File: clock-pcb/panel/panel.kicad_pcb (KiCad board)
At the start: 2 copper layers, 69.4 x 89.9 mm, 94 parts, among them J1 Conn_01x03_Pin, J1 Conn_01x07_Socket, J1 USB4140-GF-0070-C, J10 Conn_01x01_Socket, J11 Conn_01x01_Socket, J12 Conn_01x01_Socket, J13 Conn_01x01_Socket, J14 Conn_01x01_Socket, J15 Conn_01x02_Socket, J2 Conn_01x01_Pin, J2 oled, J3 Led display, J4 Led display 2, J5 Conn_01x07_Socket, J6 Conn_01x07_Socket, J7 Conn_01x01_Socket, J8 Conn_01x02_Socket, J9 Conn_01x01_Socket, Q1 FS8205A, Q2 FDN304PZ, U1 BH1750FVI-TR, U1 ESP32-WROOM-E, U1 TMAG5231C1GQDBZR, U3 OPT3004DTSR, U4 SHT4x, U4 TPS2116DRL, U5 MCP73811T-420I-OT, U7 TLV75533PDBV

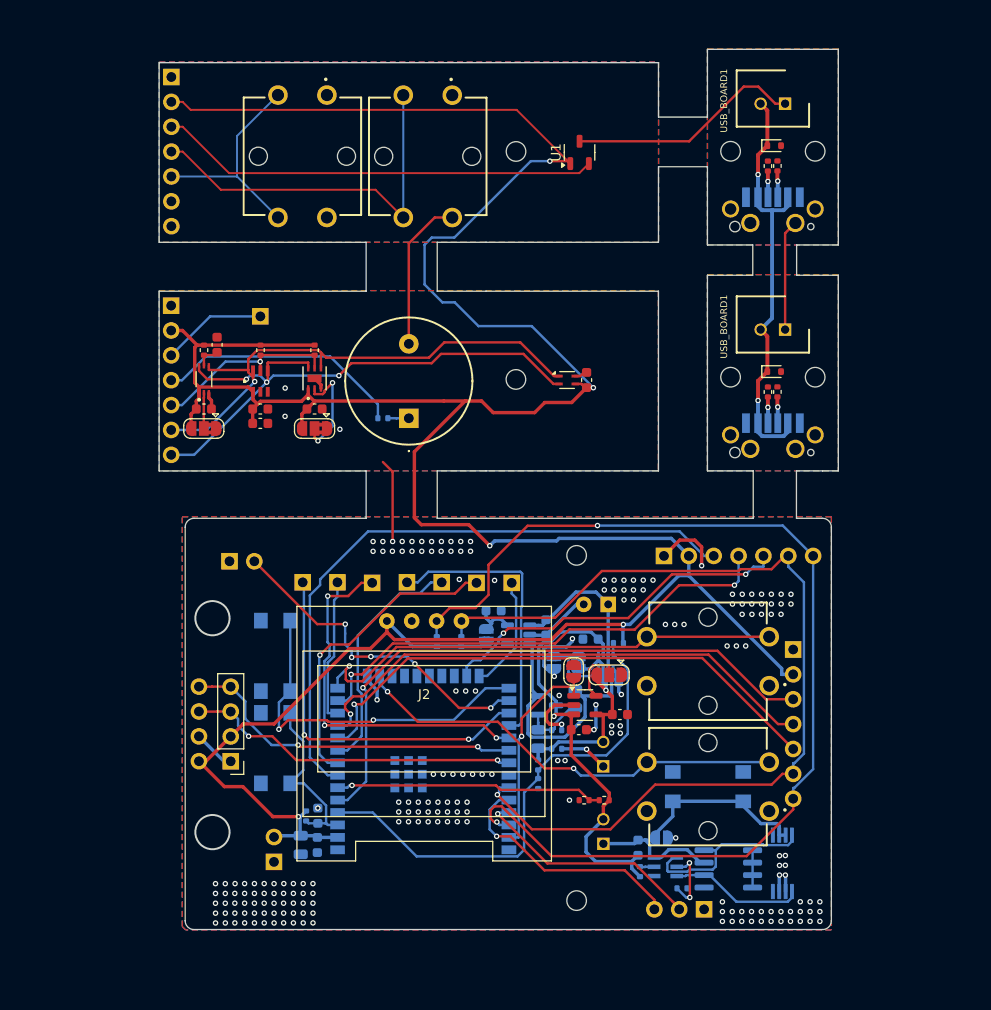
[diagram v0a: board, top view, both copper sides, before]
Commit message: voltage regulator
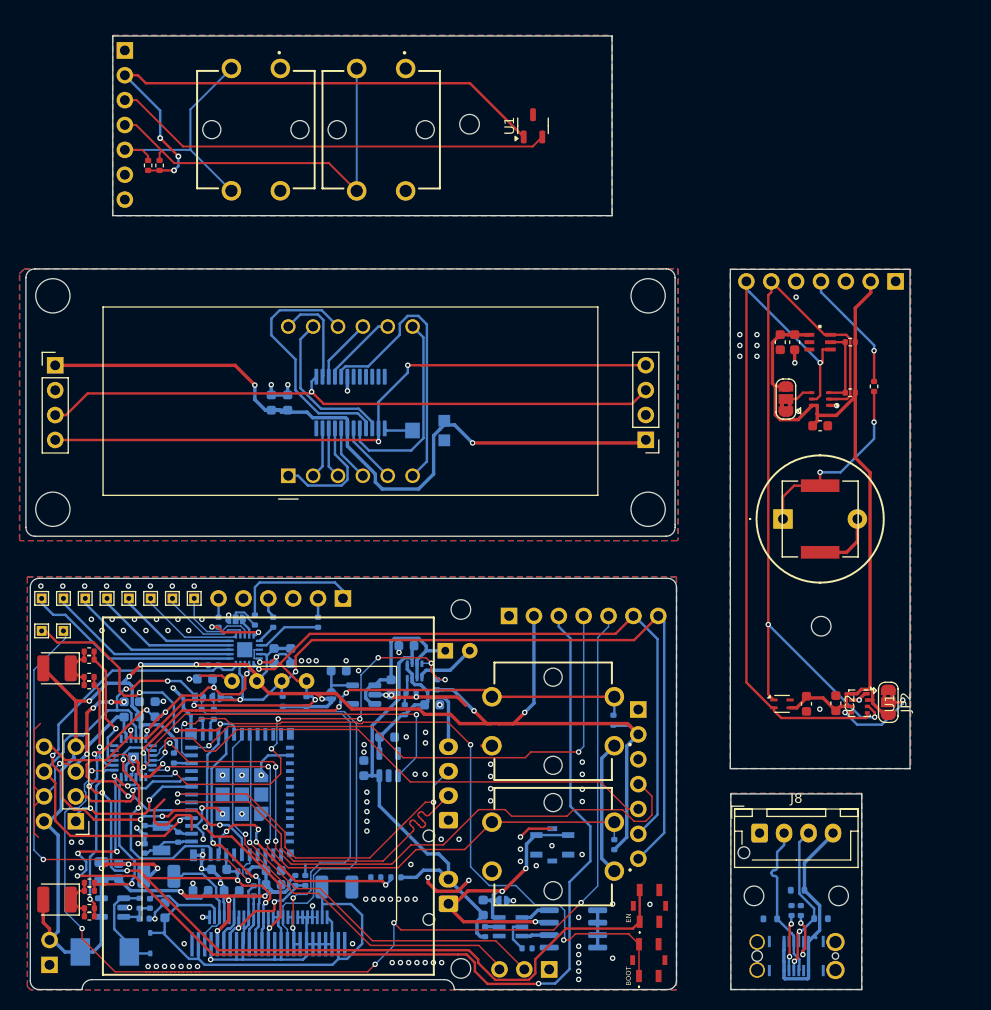
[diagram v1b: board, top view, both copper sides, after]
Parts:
- removed BATT_P1, BOOT1, EN1: TL3305AF160QG, clock:TL3305AF160QG
- removed the C1 at (110.3, 82.2)
- removed the C1 at (118.9, 133.3)
- removed the C2 at (109.0, 88.8)
- removed the C2 at (120.6, 133.3)
- removed the C3 at (114.8, 88.8)
- removed the C3 at (120.6, 130.3)
- removed the C4 at (114.8, 90.3)
- removed the C4 at (153.3, 133.6)
- removed the C5 at (120.3, 88.8)
- removed the C5 at (150.3, 108.8)
- removed the C6 at (148.1, 85.8)
- removed the C6 at (150.6, 116.7)
- removed the D1 at (167.2, 85.0)
- removed the D1 at (167.2, 61.9)
- removed the D3 at (143.1, 122.5)
- removed D4: SD0805S040S0R5, Diode_SMD:D_0805_2012Metric
- removed the J1 at (167.1, 68.6)
- removed the J1 at (167.1, 91.7)
- removed the J1 at (105.7, 78.2)
- removed the J1 at (105.7, 54.9)
- removed the J1 at (160.1, 139.9)
- removed J10, J12, J13, J14: Conn_01x01_Socket, Connector_PinSocket_2.54mm:PinSocket_1x01_P2.54mm_Vertical
- removed the J2 at (118.5, 134.9)
- removed the J2 at (114.8, 79.3)
- removed the J8 at (111.6, 104.3)
- removed the JP1 at (109.0, 90.8)
- removed the JP1 at (155.7, 132.6)
- removed the JP2 at (120.3, 90.8)
- removed the JP2 at (144.7, 114.7)
- removed JP3: Jumper_bridged, Jumper:SolderJumper-2_P1.3mm_Bridged2Bar_RoundedPad1.0x1.5mm
- removed JP4: SolderJumper_3_Open, Jumper:SolderJumper-3_P1.3mm_Open_RoundedPad1.0x1.5mm
- removed the L1 at (129.9, 89.7)
- removed Q1: FS8205A, clock:SOP65P640X120-8N
- removed Q2: FDN304PZ, Package_TO_SOT_SMD:SOT-23
- removed the R1 at (167.6, 64.0)
- removed the R1 at (109.0, 82.8)
- removed the R1 at (167.6, 87.0)
- removed the R1 at (119.4, 130.4)
- removed the R11 at (132.8, 112.5)
- removed the R2 at (166.6, 64.0)
- removed the R2 at (149.9, 128.8)
- removed the R2 at (166.6, 87.1)
- removed the R2 at (114.8, 82.8)
- removed the R3 at (120.3, 82.8)
- removed the R3 at (147.8, 128.8)
- removed the R4 at (127.3, 89.7)
- removed the R4 at (153.5, 136.1)
- removed the S1 at (119.1, 63.0)
- removed the S2 at (131.9, 63.0)
- removed the U1 at (109.0, 85.8)
- removed the U1 at (147.4, 62.6)
- removed the U1 at (131.4, 126.8)
- removed the U2 at (114.8, 85.9)
- removed the U2 at (156.1, 135.6)
- removed the U3 at (120.3, 85.7)
- removed the U3 at (149.8, 133.2)
- removed the U4 at (146.1, 85.8)
- removed the U4 at (150.0, 114.6)
- removed USB_BOARD1 (x3): Conn_01x02_Socket, clock:SHDR2W64P0X250_1X2_740X575X700P
- added C1: 0.1uF, Capacitor_SMD:C_0603_1608Metric, F.Cu at (171.9, 90.5)
- added C1: 0.1uF, Capacitor_SMD:C_0603_1608Metric, B.Cu at (116.2, 114.0)
- added C12: 1uF, Capacitor_SMD:C_0603_1608Metric, B.Cu at (104.0, 119.5)
- added C13: 1uF, Capacitor_SMD:C_0603_1608Metric, B.Cu at (110.5, 135.8)
- added C14: 1uF, Capacitor_SMD:C_0603_1608Metric, B.Cu at (109.1, 116.4)
- added C15: 1uF, Capacitor_SMD:C_0603_1608Metric, B.Cu at (117.9, 114.0)
- added C16: 4.7uF, Capacitor_SMD:C_0805_2012Metric, B.Cu at (98.5, 136.0)
- added C17: 10uF, Capacitor_SMD:C_0603_1608Metric, B.Cu at (105.0, 140.0)
- added C18: 6.4pF, Capacitor_SMD:C_0402_1005Metric, B.Cu at (103.5, 139.3)
- added C19: 19pF, Capacitor_SMD:C_0402_1005Metric, B.Cu at (103.0, 131.8)
- added C2: 0.1uF, Capacitor_SMD:C_0603_1608Metric, F.Cu at (173.5, 118.8)
- added C2: 0.1uF, Capacitor_SMD:C_0603_1608Metric, B.Cu at (100.8, 119.5)
- added C20: 19pF, Capacitor_SMD:C_0402_1005Metric, B.Cu at (103.0, 133.7)
- added C21: 1uF, Capacitor_SMD:C_0603_1608Metric, B.Cu at (100.3, 136.0)
- added C23: 0.1uF, Capacitor_SMD:C_0603_1608Metric, B.Cu at (117.5, 88.1)
- added C23: 0.1uF, Capacitor_SMD:C_0603_1608Metric, B.Cu at (116.1, 135.9)
- added C24: 10uF, Capacitor_SMD:C_0603_1608Metric, B.Cu at (115.9, 88.1)
- added C24: 10uF, Capacitor_SMD:C_0603_1608Metric, B.Cu at (116.1, 137.4)
- added C25: 1uF, Capacitor_SMD:C_0603_1608Metric, B.Cu at (111.8, 138.0)
- added C26: 4.7uF, Capacitor_Tantalum_SMD:CP_EIA-3528-12_Kemet-T, B.Cu at (104.4, 136.5)
- added C27: 4.7uF, Capacitor_Tantalum_SMD:CP_EIA-3528-12_Kemet-T, B.Cu at (122.6, 137.6)
- added C28: 1uF, Capacitor_SMD:C_0603_1608Metric, B.Cu at (108.7, 138.0)
- added C3: 0.1uF, Capacitor_SMD:C_0603_1608Metric, F.Cu at (169.3, 82.0)
- added C3: 10uF, Capacitor_SMD:C_0603_1608Metric, B.Cu at (102.4, 119.5)
- added C4: 4.7uF, Capacitor_SMD:C_0603_1608Metric, F.Cu at (167.9, 82.0)
- added C4: 0.1uF, Capacitor_SMD:C_0603_1608Metric, B.Cu at (137.5, 139.7)
- added C5: 100uF, Capacitor_THT:CP_Radial_D5.0mm_P2.50mm, B.Cu at (133.6, 113.5)
- added C6: 0.1uF, Capacitor_SMD:C_0603_1608Metric, F.Cu at (170.5, 118.9)
- added C6: 1uF, Capacitor_SMD:C_0603_1608Metric, B.Cu at (132.3, 119.0)
- added D1: LED, LED_SMD:LED_1210_3225Metric, F.Cu at (94.0, 138.9)
- added D1: ESD5Zxx, Diode_SMD:D_SOD-523, B.Cu at (169.6, 138.0)
- added D2: LED, LED_SMD:LED_1210_3225Metric, F.Cu at (94.0, 115.3)
- added D2: ESD5Zxx, Diode_SMD:D_SOD-523, B.Cu at (166.8, 140.9)
- added D3: ESD5Zxx, Diode_SMD:D_SOD-523, B.Cu at (172.0, 140.9)
- added D3: NSVR0340HT1G, Diode_SMD:D_SOD-323, B.Cu at (103.5, 143.4)
- added IC1: VEML6030-GS15, clock:VEML6030GS15, F.Cu at (171.9, 87.8)
- added IC2: MCP23018-E_MJ, clock:QFN50P400X400X90-25N-D, B.Cu at (101.8, 124.4)
- added J1: Conn_01x04_Socket, Connector_PinHeader_2.54mm:PinHeader_1x04_P2.54mm_Vertical, F.Cu at (93.8, 84.3)
- added J1: Conn_01x03_Pin, Connector_PinHeader_2.54mm:PinHeader_1x03_P2.54mm_Vertical, B.Cu at (144.3, 146.0)
- added J1: Conn_01x07_Socket, Connector_PinHeader_2.54mm:PinHeader_1x07_P2.54mm_Horizontal, B.Cu at (179.6, 75.8)
- added J1: Conn_01x07_Socket, Connector_PinHeader_2.54mm:PinHeader_1x07_P2.54mm_Horizontal, B.Cu at (100.9, 52.2)
- added J1: USB4145-03-0070-C, clock:USB4145030070C, B.Cu at (169.5, 144.7)
- added J2: oled 2, clock:SSD1306_0.96_Oled, F.Cu at (102.7, 141.1)
- added J2: Conn_01x04_Socket, Connector_PinHeader_2.54mm:PinHeader_1x04_P2.54mm_Vertical, F.Cu at (154.1, 91.9)
- added J8: Conn_01x04_Socket, Connector_JST:JST_XH_B4B-XH-AM_1x04_P2.50mm_Vertical, F.Cu at (165.8, 132.1)
- added J8: SFV25R-2STE1HLF, clock:AMPHENOL_SFV25R-2STE1HLF, B.Cu at (115.6, 143.1)
- added JP1: SolderJumper_3_Bridged12, Jumper:SolderJumper-3_P1.3mm_Bridged2Bar12_RoundedPad1.0x1.5mm, F.Cu at (168.4, 87.8)
- added JP1: Jumper, clock:jumper_solder_small, B.Cu at (139.5, 139.0)
- added JP2: SolderJumper_3_Bridged12, Jumper:SolderJumper-3_P1.3mm_Bridged2Bar12_RoundedPad1.0x1.5mm, F.Cu at (178.9, 118.8)
- added JP2: SolderJumper_3_Bridged12, clock:jumper_solder_small_3_bridged, B.Cu at (112.2, 110.3)
- added JP6: Jumper, clock:jumper_solder_small, B.Cu at (110.3, 118.2)
- added L1: CPT-14146-80T, clock:CPT1414680T, F.Cu at (168.1, 100.0)
- added L1: 10uH 1A, clock:HPI0530-100, B.Cu at (98.9, 144.0)
- added LS1: Speaker_Crystal, clock:AST0760_MAL, F.Cu at (171.9, 100.0)
- added R0: 5.1k, Resistor_SMD:R_0402_1005Metric, B.Cu at (105.9, 124.5)
- added R1: 10K, Resistor_SMD:R_0402_1005Metric, F.Cu at (104.5, 63.9)
- added R1: 10K, Resistor_SMD:R_0402_1005Metric, F.Cu at (175.0, 87.1)
- added R1: 100k, Resistor_SMD:R_0402_1005Metric, B.Cu at (117.0, 118.7)
- added R1: 5.1k, Resistor_SMD:R_0402_1005Metric, B.Cu at (170.0, 140.0)
- added R11: 10K, Resistor_SMD:R_0402_1005Metric, F.Cu at (103.3, 63.9)
- added R11: 10K, Resistor_SMD:R_0402_1005Metric, B.Cu at (113.0, 136.0)
- added R13: 250k, Resistor_SMD:R_0402_1005Metric, B.Cu at (129.5, 119.5)
- added R14: 100k, Resistor_SMD:R_0402_1005Metric, B.Cu at (130.2, 117.8)
- added R15: 10K, Resistor_SMD:R_0402_1005Metric, B.Cu at (150.8, 120.6)
- added R16: 10K, Resistor_SMD:R_0402_1005Metric, B.Cu at (120.7, 110.6)
- added R17: 330, Resistor_SMD:R_0402_1005Metric, F.Cu at (97.3, 137.2)
- added R18: 330, Resistor_SMD:R_0402_1005Metric, F.Cu at (97.3, 140.6)
- added R19: 330, Resistor_SMD:R_0402_1005Metric, F.Cu at (97.3, 138.0)
- added R2: 10K, Resistor_SMD:R_0402_1005Metric, F.Cu at (175.0, 82.0)
- added R2: 300k, Resistor_SMD:R_0402_1005Metric, B.Cu at (128.6, 136.6)
- added R20: 330, Resistor_SMD:R_0402_1005Metric, F.Cu at (97.3, 139.8)
- added R21: 10M, Resistor_SMD:R_0402_1005Metric, B.Cu at (106.4, 132.5)
- added R22: 330, Resistor_SMD:R_0402_1005Metric, F.Cu at (97.3, 116.2)
- added R23: 330, Resistor_SMD:R_0402_1005Metric, F.Cu at (97.3, 117.0)
- added R24: 330, Resistor_SMD:R_0402_1005Metric, F.Cu at (97.3, 114.4)
- added R25: 330, Resistor_SMD:R_0402_1005Metric, F.Cu at (97.3, 113.6)
- added R26: 300k, Resistor_SMD:R_0402_1005Metric, B.Cu at (102.9, 140.8)
- added R27: 3.16M, Resistor_SMD:R_0402_1005Metric, B.Cu at (102.4, 139.3)
- added R28: 10K, Resistor_SMD:R_0402_1005Metric, B.Cu at (150.9, 133.3)
- added R29: 1.2M, Resistor_SMD:R_0402_1005Metric, B.Cu at (114.1, 138.0)
- added R3: 800k, Resistor_SMD:R_0402_1005Metric, B.Cu at (126.5, 136.6)
- added R3: 5.1k, Resistor_SMD:R_0402_1005Metric, B.Cu at (169.0, 140.0)
- added R30: 10K, Resistor_SMD:R_0402_1005Metric, B.Cu at (119.3, 136.9)
- added R31: 10K, Resistor_SMD:R_0402_1005Metric, B.Cu at (118.3, 136.9)
- added R32: N/A, Resistor_SMD:R_0402_1005Metric, B.Cu at (110.0, 120.0)
- added R33: N/A, Resistor_SMD:R_0402_1005Metric, B.Cu at (108.8, 120.0)
- added R4: 330R, Resistor_SMD:R_0402_1005Metric, F.Cu at (177.4, 86.5)
- added R4: 330R, Resistor_SMD:R_0402_1005Metric, B.Cu at (137.7, 142.2)
- added S1: B3F-5050, clock:B3F-4055, F.Cu at (114.3, 60.3)
- added S1: TS21-34-035-BK-160-SMT-TR, clock:TS2134035BK160SMTTR, F.Cu at (154.4, 145.1)
- added S2: TS21-34-035-BK-160-SMT-TR, clock:TS2134035BK160SMTTR, F.Cu at (154.5, 139.5)
- added S2: B3F-5050, clock:B3F-4055, F.Cu at (127.1, 60.3)
- added S5: TS21-34-035-BK-160-SMT-TR, clock:TS2134035BK160SMTTR, B.Cu at (144.6, 133.3)
- added TP1: TestPoint, TestPoint:TestPoint_THTPad_1.0x1.0mm_Drill0.5mm, F.Cu at (92.4, 111.5)
- added TP12: TestPoint, TestPoint:TestPoint_THTPad_1.0x1.0mm_Drill0.5mm, F.Cu at (105.8, 108.1)
- added TP13: TestPoint, TestPoint:TestPoint_THTPad_1.0x1.0mm_Drill0.5mm, F.Cu at (108.0, 108.1)
- added TP3: TestPoint, TestPoint:TestPoint_THTPad_1.0x1.0mm_Drill0.5mm, F.Cu at (92.4, 108.1)
- added TP4: TestPoint, TestPoint:TestPoint_THTPad_1.0x1.0mm_Drill0.5mm, F.Cu at (94.6, 108.1)
- added TP5: TestPoint, TestPoint:TestPoint_THTPad_1.0x1.0mm_Drill0.5mm, F.Cu at (96.9, 108.1)
- added TP6: TestPoint, TestPoint:TestPoint_THTPad_1.0x1.0mm_Drill0.5mm, F.Cu at (99.1, 108.1)
- added TP7: TestPoint, TestPoint:TestPoint_THTPad_1.0x1.0mm_Drill0.5mm, F.Cu at (101.3, 108.1)
- added TP8: TestPoint, TestPoint:TestPoint_THTPad_1.0x1.0mm_Drill0.5mm, F.Cu at (103.5, 108.1)
- added TP9: TestPoint, TestPoint:TestPoint_THTPad_1.0x1.0mm_Drill0.5mm, F.Cu at (94.6, 111.5)
- added U1: CC56-12EWA, Display_7Segment:CA56-12EWA, F.Cu at (117.6, 95.6)
- added U1: BMP280, Package_LGA:Bosch_LGA-8_2x2.5mm_P0.65mm_ClockwisePinNumbering, F.Cu at (175.9, 118.8)
- added U1: TMAG5231C1GQDBZR, Package_TO_SOT_SMD:SOT-23-3, F.Cu at (142.6, 59.9)
- added U1: ESP32-C6-MINI-1-N4, clock:XCVR_ESP32-C6-MINI-1-N4, B.Cu at (112.9, 128.2)
- added U2: ~, clock:LTR-F216A, F.Cu at (171.9, 82.0)
- added U2: AS1115-BSST, Package_SO:QSOP-24_3.9x8.7mm_P0.635mm, B.Cu at (124.0, 88.1)
- added U2: ~, clock:SOT95P280X140-6N, B.Cu at (140.3, 141.7)
- added U3: ~, Connector_JST:JST_XH_B2B-XH-AM_1x02_P2.50mm_Vertical, B.Cu at (134.0, 139.3)
- added U4: SHT4x, clock:Sensirion_DFN-4_1.5x1.5mm_P0.8mm_SHT4x_NoCentralPad, F.Cu at (168.0, 118.9)
- added U4: TPS2116DRL, Package_TO_SOT_SMD:SOT-583-8, B.Cu at (130.5, 115.5)
- added U6: TPS61040DBV, Package_TO_SOT_SMD:SOT-23-5, B.Cu at (99.7, 139.7)
- added U8: AT42QT2120-MMHR, clock:QFN45P300X300X85-21N, B.Cu at (113.2, 113.4)
- added VR1: TC33X-2-303E, LIB_TC33X-2-303E:TC33X2304E, B.Cu at (131.7, 91.0)
- added Y2: 32.768KHz, clock:XTAL_9HT10_TXC, B.Cu at (104.7, 132.6)
- C10, C11, U5: moved to B.Cu
- J11: value Conn_01x01_Socket -> Conn_01x06_Socket; footprint Connector_PinSocket_2.54mm:PinSocket_1x01_P2.54mm_Vertical -> Connector_PinHeader_2.54mm:PinHeader_1x06_P2.54mm_Vertical
- J5, J6: footprint Connector_PinSocket_2.54mm:PinSocket_1x07_P2.54mm_Vertical -> Connector_PinHeader_2.54mm:PinHeader_1x07_P2.54mm_Vertical
- J7: value Conn_01x01_Socket -> SFV25R-2STE1HLF; footprint Connector_PinSocket_2.54mm:PinSocket_1x01_P2.54mm_Vertical -> clock:OLED_1.5IN_128X128MONO; moved to F.Cu
- J9: value Conn_01x01_Socket -> Conn_01x04_Socket; footprint Connector_PinSocket_2.54mm:PinSocket_1x01_P2.54mm_Vertical -> Connector_JST:JST_XH_B4B-XH-AM_1x04_P2.50mm_Vertical
- JP5: value SolderJumper_2_Open -> Jumper; footprint Jumper:SolderJumper-2_P1.3mm_Open_RoundedPad1.0x1.5mm -> clock:jumper_solder_small; moved to B.Cu
- JP7: footprint Jumper:SolderJumper-2_P1.3mm_Open_RoundedPad1.0x1.5mm -> clock:jumper_solder_small
- R10: value 800k -> 10K
- R12: value 5.1k -> 100k
- R7: value 500k -> 47K
- R8: value 100K -> 10K
- R9: value 50k -> 10K
- moved JP5 38.4 mm to (108.5, 118.3), turned to 0 degrees
- moved R8 36.3 mm to (110.5, 110.6), turned to -90 degrees
- moved R7 34.7 mm to (110.0, 115.0), turned to 0 degrees
- moved R9 33.5 mm to (114.2, 110.3), turned to -90 degrees
- moved R10 31.7 mm to (116.1, 110.6)
- moved J7 30.4 mm to (115.6, 128.3), turned to 0 degrees
- moved J9 25.5 mm to (134.0, 130.8)
- moved J15 25.2 mm to (93.2, 145.6)
- moved C10 23.9 mm to (127.7, 122.3)
- moved C11 22.3 mm to (125.3, 125.5), turned to 90 degrees
- moved U5 20.9 mm to (127.9, 125.1), turned to 90 degrees
- moved R6 19.0 mm to (132.8, 117.0), turned to -90 degrees
- moved C7 18.8 mm to (129.7, 113.0)
- moved R12 17.0 mm to (119.5, 118.7)
- moved C8 17.0 mm to (122.8, 115.5)
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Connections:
- AO9926C1 pad 2: CO -> Net-(AO9926C1-G2)
- AO9926C1 pad 4: DO -> Net-(AO9926C1-G1)
- J3 pad 1: CLK -> SCL
- J3 pad 2: DIO -> SDA
- J4 pad 1: GND -> CLK
- J4 pad 2: +3V3 -> DIO
- J4 pad 3: DIO -> GND
- J4 pad 4: CLK -> +3V3
- J5 pad 3: GPIO35 -> SUB_TOP_3
- J5 pad 4: GPIO14 -> BUZZER
- J5 pad 5: GPIO15 -> SUB_TOP_1
- J6 pad 3: GPIO39 -> HALL_SENS
- J6 pad 4: GPIO26 -> BUTTON_EXIT
- J6 pad 5: GPIO25 -> BUTON_CONF
- J7 pad 1: Net-(J7-Pin_1) -> GND
- J9 pad 1: Net-(J9-Pin_1) -> GND
- JP5 pad 1: GND -> SDA
- JP5 pad 2: CHARGE_EN -> MOSI
- R10 pad 1: POWER_STATUS -> Net-(J11-Pin_4)
- R10 pad 2: GND -> SLID_1
- R7 pad 1: VBUS -> +3V3
- R7 pad 2: POWER_STATUS -> TOUCH_INT
- R8 pad 1: Net-(D3-K) -> Net-(J11-Pin_6)
- R8 pad 2: GND -> SLID_2
- R9 pad 1: VBUS -> Net-(J11-Pin_1)
- R9 pad 2: GND -> GUARD
- U5 pad 5: Net-(JP4-C) -> GND
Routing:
- net SDA: track 151.5 -> 275.6 mm, vias 2 -> 9
- net SUB_TOP_1: track 0.00 -> 114.5 mm, vias 0 -> 6
- net SUB_TOP_3: track 0.00 -> 112.7 mm, vias 0 -> 6
- net EN: track 18.1 -> 128.8 mm, vias 0 -> 11
- net GPIO35: track 110.5 -> 0.00 mm
- net BUTTON_EXIT: track 0.00 -> 109.4 mm, vias 0 -> 3
- net GND: track 112.4 -> 205.9 mm, vias 205 -> 146
- net GPIO14: track 88.9 -> 0.00 mm, vias 2 -> 0
- net SCL: track 172.4 -> 260.0 mm, vias 5 -> 7
- net BUTON_CONF: track 0.00 -> 82.0 mm, vias 0 -> 1
- net GPIO26: track 79.9 -> 0.00 mm, vias 1 -> 0
- net +3.3V: track 0.00 -> 76.3 mm, vias 0 -> 2
- net GPIO9: track 0.00 -> 73.6 mm, vias 0 -> 3
- net GPIO39: track 71.7 -> 0.00 mm, vias 1 -> 0
- net BUZZER: track 0.00 -> 68.6 mm, vias 0 -> 3
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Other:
- board size 69.4 x 89.9 mm -> 90.3 x 97.4 mm
- board text added: "BOOT"
- board text added: "EN"
- board text removed: "3.3V"
- board text removed: "GND"
- board text removed: "GPIO16"
- board text removed: "GPIO17"
- board text removed: "GPIO2"
- board text removed: "GPIO27"
- board text removed: "GPIO32"
- board text removed: "GPIO33"
- board text removed: "GPIO4_T"
- board text removed: "GPIO5"

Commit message: panel
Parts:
- removed the C1 at (171.9, 90.5)
- removed the C1 at (116.2, 114.0)
- removed the C13 at (110.5, 135.8)
- removed the C2 at (173.5, 118.8)
- removed the C2 at (100.8, 119.5)
- removed the C23 at (117.5, 88.1)
- removed the C23 at (116.1, 135.9)
- removed the C24 at (115.9, 88.1)
- removed the C24 at (116.1, 137.4)
- removed the C3 at (169.3, 82.0)
- removed the C3 at (102.4, 119.5)
- removed the C4 at (167.9, 82.0)
- removed the C4 at (137.5, 139.7)
- removed the C5 at (133.6, 113.5)
- removed the C6 at (170.5, 118.9)
- removed the C6 at (132.3, 119.0)
- removed the C7 at (129.7, 113.0)
- removed the D1 at (94.0, 138.9)
- removed the D1 at (169.6, 138.0)
- removed the D2 at (94.0, 115.3)
- removed the D2 at (166.8, 140.9)
- removed the D3 at (172.0, 140.9)
- removed the D3 at (103.5, 143.4)
- removed the J1 at (93.8, 84.3)
- removed the J1 at (144.3, 146.0)
- removed the J1 at (179.6, 75.8)
- removed the J1 at (100.9, 52.2)
- removed the J1 at (169.5, 144.7)
- removed the J2 at (102.7, 141.1)
- removed the J2 at (154.1, 91.9)
- removed the J8 at (165.8, 132.1)
- removed the J8 at (115.6, 143.1)
- removed the JP1 at (168.4, 87.8)
- removed the JP1 at (139.5, 139.0)
- removed the JP2 at (178.9, 118.8)
- removed the JP2 at (112.2, 110.3)
- removed the L1 at (168.1, 100.0)
- removed the L1 at (98.9, 144.0)
- removed the R1 at (104.5, 63.9)
- removed the R1 at (175.0, 87.1)
- removed the R1 at (117.0, 118.7)
- removed the R1 at (170.0, 140.0)
- removed the R11 at (103.3, 63.9)
- removed the R11 at (113.0, 136.0)
- removed the R2 at (175.0, 82.0)
- removed the R2 at (128.6, 136.6)
- removed the R3 at (126.5, 136.6)
- removed the R3 at (169.0, 140.0)
- removed the R4 at (177.4, 86.5)
- removed the R4 at (137.7, 142.2)
- removed the R5 at (142.0, 143.9)
- removed the R6 at (132.8, 117.0)
- removed the S1 at (114.3, 60.3)
- removed the S1 at (154.4, 145.1)
- removed the S2 at (154.5, 139.5)
- removed the S2 at (127.1, 60.3)
- removed the U1 at (117.6, 95.6)
- removed the U1 at (175.9, 118.8)
- removed the U1 at (142.6, 59.9)
- removed the U1 at (112.9, 128.2)
- removed the U2 at (171.9, 82.0)
- removed the U2 at (124.0, 88.1)
- removed the U2 at (140.3, 141.7)
- removed the U3 at (134.0, 139.3)
- removed the U4 at (168.0, 118.9)
- removed the U4 at (130.5, 115.5)
- added C1: 0.1uF, Capacitor_SMD:C_0603_1608Metric, F.Cu at (114.1, 52.4)
- added C1: 0.1uF, Capacitor_SMD:C_0603_1608Metric, B.Cu at (116.2, 113.7)
- added C13: 1uF, Capacitor_SMD:C_0603_1608Metric, F.Cu at (104.4, 58.3)
- added C13: 1uF, Capacitor_SMD:C_0603_1608Metric, B.Cu at (110.6, 135.5)
- added C2: 0.1uF, Capacitor_SMD:C_0603_1608Metric, F.Cu at (145.2, 56.6)
- added C2: 0.1uF, Capacitor_SMD:C_0603_1608Metric, B.Cu at (100.9, 119.1)
- added C22: 6.4pF, Capacitor_SMD:C_01005_0402Metric, B.Cu at (104.5, 139.1)
- added C23: 0.1uF, Capacitor_SMD:C_0603_1608Metric, B.Cu at (130.9, 86.0)
- added C23: 0.1uF, Capacitor_SMD:C_0603_1608Metric, B.Cu at (116.2, 135.6)
- added C24: 10uF, Capacitor_SMD:C_0603_1608Metric, B.Cu at (116.2, 137.0)
- added C24: 10uF, Capacitor_SMD:C_0603_1608Metric, B.Cu at (132.6, 86.0)
- added C3: 0.1uF, Capacitor_SMD:C_0603_1608Metric, F.Cu at (116.6, 61.7)
- added C3: 10uF, Capacitor_SMD:C_0603_1608Metric, B.Cu at (102.5, 119.1)
- added C4: 4.7uF, Capacitor_SMD:C_0603_1608Metric, F.Cu at (118.0, 61.7)
- added C4: 0.1uF, Capacitor_SMD:C_0603_1608Metric, B.Cu at (137.6, 139.4)
- added C5: 1uF, Capacitor_SMD:C_0603_1608Metric, F.Cu at (110.8, 58.3)
- added C5: 100uF, Capacitor_THT:CP_Radial_D5.0mm_P2.50mm, B.Cu at (134.7, 113.2)
- added C6: 0.1uF, Capacitor_SMD:C_0603_1608Metric, F.Cu at (145.3, 59.6)
- added C6: 1uF, Capacitor_SMD:C_0603_1608Metric, B.Cu at (132.4, 118.7)
- added C7: 1uF, Capacitor_SMD:C_0603_1608Metric, B.Cu at (129.7, 112.6)
- added C7: 100uF, Capacitor_THT:CP_Radial_D5.0mm_P2.50mm, B.Cu at (105.8, 61.2)
- added D1: LED, LED_SMD:LED_1210_3225Metric, F.Cu at (94.0, 138.6)
- added D1: ESD5Zxx, Diode_SMD:D_SOD-523, B.Cu at (177.6, 82.5)
- added D2: LED, LED_SMD:LED_1210_3225Metric, F.Cu at (94.0, 114.9)
- added D2: ESD5Zxx, Diode_SMD:D_SOD-523, B.Cu at (174.8, 85.5)
- added D3: NSVR0340HT1G, Diode_SMD:D_SOD-323, B.Cu at (103.6, 143.0)
- added D3: ESD5Zxx, Diode_SMD:D_SOD-523, B.Cu at (180.0, 85.4)
- added J1: Conn_01x04_Socket, Connector_PinHeader_2.54mm:PinHeader_1x04_P2.54mm_Vertical, F.Cu at (154.6, 89.8)
- added J1: Conn_01x07_Socket, Connector_PinHeader_2.54mm:PinHeader_1x07_P2.54mm_Horizontal, B.Cu at (102.1, 50.5)
- added J1: Conn_01x07_Socket, Connector_PinHeader_2.54mm:PinHeader_1x07_P2.54mm_Horizontal, B.Cu at (170.4, 146.8)
- added J1: Conn_01x03_Pin, Connector_PinHeader_2.54mm:PinHeader_1x03_P2.54mm_Vertical, B.Cu at (144.3, 145.7)
- added J1: USB4145-03-0070-C, clock:USB4145030070C, B.Cu at (177.5, 89.2)
- added J2: Conn_01x04_Socket, Connector_PinHeader_2.54mm:PinHeader_1x04_P2.54mm_Vertical, F.Cu at (94.3, 82.2)
- added J2: oled 2, clock:SSD1306_0.96_Oled, F.Cu at (102.7, 140.7)
- added J8: Conn_01x04_Socket, Connector_JST:JST_XH_B4B-XH-AM_1x04_P2.50mm_Vertical, F.Cu at (173.8, 76.7)
- added J8: SFV25R-2STE1HLF, clock:AMPHENOL_SFV25R-2STE1HLF, B.Cu at (115.6, 142.8)
- added JP1: SolderJumper_3_Bridged12, Jumper:SolderJumper-3_P1.3mm_Bridged2Bar12_RoundedPad1.0x1.5mm, F.Cu at (117.6, 55.3)
- added JP1: Jumper, clock:jumper_solder_small, B.Cu at (139.6, 138.7)
- added JP2: SolderJumper_3_Bridged12, Jumper:SolderJumper-3_P1.3mm_Bridged2Bar12_RoundedPad1.0x1.5mm, F.Cu at (145.1, 51.0)
- added JP2: SolderJumper_3_Bridged12, clock:jumper_solder_small_3_bridged, B.Cu at (112.3, 109.9)
- added L1: CPT-14146-80T, clock:CPT1414680T, F.Cu at (126.4, 62.1)
- added L1: 10uH 1A, clock:HPI0530-100, B.Cu at (98.9, 143.7)
- added R1: 10K, Resistor_SMD:R_0402_1005Metric, F.Cu at (182.2, 143.3)
- added R1: 10K, Resistor_SMD:R_0402_1005Metric, F.Cu at (111.0, 56.0)
- added R1: 100k, Resistor_SMD:R_0402_1005Metric, B.Cu at (117.1, 118.3)
- added R1: 5.1k, Resistor_SMD:R_0402_1005Metric, B.Cu at (178.0, 84.6)
- added R11: 10K, Resistor_SMD:R_0402_1005Metric, F.Cu at (182.2, 144.4)
- added R11: 10K, Resistor_SMD:R_0402_1005Metric, B.Cu at (113.0, 135.7)
- added R2: 10K, Resistor_SMD:R_0402_1005Metric, F.Cu at (111.0, 61.7)
- added R2: 300k, Resistor_SMD:R_0402_1005Metric, B.Cu at (128.6, 136.3)
- added R3: 10K, Resistor_SMD:R_0402_1005Metric, F.Cu at (107.9, 61.6)
- added R3: 5.1k, Resistor_SMD:R_0402_1005Metric, B.Cu at (177.0, 84.6)
- added R3: 800k, Resistor_SMD:R_0402_1005Metric, B.Cu at (126.6, 136.3)
- added R4: 330R, Resistor_SMD:R_0402_1005Metric, F.Cu at (114.0, 50.4)
- added R4: 330R, Resistor_SMD:R_0402_1005Metric, B.Cu at (137.8, 141.8)
- added R5: 22R, Resistor_SMD:R_0402_1005Metric, F.Cu at (108.9, 55.6)
- added R5: 2.7K, Resistor_SMD:R_0402_1005Metric, B.Cu at (142.0, 143.5)
- added R6: 10K, Resistor_SMD:R_0402_1005Metric, B.Cu at (132.8, 116.4)
- added R6: 22R, Resistor_THT:R_Axial_DIN0204_L3.6mm_D1.6mm_P2.54mm_Vertical, B.Cu at (107.2, 53.1)
- added REF**: R_0805_2012Metric, Resistor_SMD:R_0805_2012Metric, B.Cu at (177.5, 100.1)
- added S1: B3F-5050, clock:B3F-4055, F.Cu at (178.5, 133.4)
- added S1: TS21-34-035-BK-160-SMT-TR, clock:TS2134035BK160SMTTR, F.Cu at (154.5, 144.7)
- added S2: B3F-5050, clock:B3F-4055, F.Cu at (178.5, 120.6)
- added S2: TS21-34-035-BK-160-SMT-TR, clock:TS2134035BK160SMTTR, F.Cu at (154.5, 139.2)
- added TP10: TestPoint, TestPoint:TestPoint_THTPad_1.0x1.0mm_Drill0.5mm, F.Cu at (96.9, 111.1)
- added TP2: TestPoint, TestPoint:TestPoint_Pad_D1.0mm, B.Cu at (104.9, 145.1)
- added U1: BMP280, clock:Bosch_LGA-8_2x2.5mm_P0.65mm_ClockwisePinNumbering, F.Cu at (145.2, 54.2)
- added U1: CC56-12EWA, Display_7Segment:CA56-12EWA, F.Cu at (130.8, 78.5)
- added U1: TMAG5231C1GQDBZR, Package_TO_SOT_SMD:SOT-23-3, F.Cu at (178.1, 105.1)
- added U1: ESP32-C6-MINI-1-N4, clock:XCVR_ESP32-C6-MINI-1-N4, B.Cu at (112.9, 127.8)
- added U2: ~, clock:LTR-F216A, F.Cu at (114.1, 61.7)
- added U2: AS1115-BSST, Package_SO:QSOP-24_3.9x8.7mm_P0.635mm, B.Cu at (124.5, 86.0)
- added U2: ~, clock:SOT95P280X140-6N, B.Cu at (140.4, 141.3)
- added U3: APDS-9960, clock:Avago_APDS-9960, F.Cu at (107.4, 58.3)
- added U3: ~, Connector_JST:JST_XH_B2B-XH-AM_1x02_P2.50mm_Vertical, B.Cu at (134.0, 139.0)
- added U4: SHT4x, clock:Sensirion_DFN-4_1.5x1.5mm_P0.8mm_SHT4x_NoCentralPad, F.Cu at (145.3, 62.1)
- added U4: TPS2116DRL, Package_TO_SOT_SMD:SOT-583-8, B.Cu at (130.6, 115.2)
- J4: footprint Connector_PinHeader_2.54mm:PinHeader_1x04_P2.54mm_Vertical -> clock:PinHeader_1x04_P2.54mm_Vertical
- U7: footprint Package_TO_SOT_SMD:SOT-23-5 -> clock:TLV75733PDYDR
- moved IC1 66.4 mm to (114.1, 55.3), turned to 0 degrees
- moved LS1 61.8 mm to (126.4, 58.3), turned to 0 degrees
- moved VR1 17.0 mm to (116.7, 83.2), turned to 90 degrees
- moved C17 0.88 mm to (105.8, 139.6)
- moved R30 0.36 mm to (119.3, 136.6)
- moved C16 0.35 mm to (98.6, 135.7)
- moved C19 0.35 mm to (103.0, 131.5)
- moved C20 0.35 mm to (103.0, 133.3)
- moved C27 0.35 mm to (122.6, 137.3)
- moved R18 0.35 mm to (97.3, 140.3)
- moved S4 0.35 mm to (144.7, 133.1)
- moved S5 0.35 mm to (144.6, 133.0)
- moved C18 0.35 mm to (103.5, 139.0)
- moved AO9926C1 0.35 mm to (146.8, 141.5)
- moved C11 0.35 mm to (125.4, 125.1)
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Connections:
- IC1 pad 3: GPIO25 -> SUB_TOP_1
- IC2 pad 13: unconnected-(IC2-INTB-Pad13) -> INT_A
- IC2 pad 4: unconnected-(IC2-GPB4-Pad4) -> HALL_SENS
- IC2 pad 6: unconnected-(IC2-GPB6-Pad6) -> Net-(IC2-GPB6)
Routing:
- net GND: track 205.9 -> 352.4 mm, vias 146 -> 593
- net SDA: track 275.6 -> 382.7 mm, vias 9 -> 16
- net HALL_SENS: track 45.0 -> 151.8 mm, vias 0 -> 6
- net SCL: track 260.0 -> 354.0 mm, vias 7 -> 8
- net +3V3: track 364.7 -> 407.2 mm
- net Net-(IC2-GPB6): track 0.00 -> 21.5 mm, vias 0 -> 1
- net SUB_TOP_1: track 114.5 -> 131.8 mm, vias 6 -> 8
- net SUB_TOP_3: track 112.7 -> 124.5 mm, vias 6 -> 8
- net GPIO25: track 8.37 -> 0.00 mm
- net Net-(U3-VDD): track 0.00 -> 7.86 mm, vias 0 -> 1
- net VBUS: track 43.5 -> 51.1 mm
- net POWER_STATUS: track 46.7 -> 51.7 mm, vias 7 -> 6
- net BUZZER: track 68.6 -> 72.8 mm
- net 14V_OLED: track 48.5 -> 51.7 mm
- net BUZZER_IN: track 19.7 -> 22.6 mm
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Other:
- board size 90.3 x 97.4 mm -> 96 x 99 mm
